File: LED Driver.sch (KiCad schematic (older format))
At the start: 0 parts

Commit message: M3 U7
LED Driver
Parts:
- added C? (x2): C, ~, symbol C
- added D?: DIODESCH, ~, symbol DIODESCH
- added L?: INDUCTOR, ~, symbol INDUCTOR
- added R?: R, ~, symbol R
- added U?: AP5726, symbol AP5726
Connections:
- net String +: now also C?.1, D?.2 (K), U?.5 (OVP)
- net String -: now also R?.1, U?.3 (FB)
- new net: D?.1 (A), L?.2, U?.1 (SW)
- new net +5V: C?.1, L?.1, U?.6 (VIN)
- new net GND: C?.2, C?.2, R?.2, U?.2 (GMND)
- new net LED_EN_PWM: U?.4 (EN)
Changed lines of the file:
@@
 Comment4 ""
 $EndDescr
-Text HLabel 1900 2500 0    60   Input ~ 0
-EN
-Text HLabel 1900 2850 0    60   Input ~ 0
-FREQ
-Text HLabel 3600 2550 0    60   Output ~ 0
+Text HLabel 1800 2000 0    60   Input ~ 0
+LED_EN_PWM
+Text HLabel 10300 900  2    60   Output ~ 0
 String +
-Text HLabel 3600 2800 0    60   Input ~ 0
+Text HLabel 10300 2350 2    60   Input ~ 0
 String -
+$Comp
+L AP5726 U?
+U 1 1 52FE2415
+P 2850 2000
+F 0 "U?" H 3050 1550 60  0000 C CNN
+F 1 "AP5726" H 2850 2050 60  0000 C CNN
+F 2 "" H 2850 2000 60  0000 C CNN
+F 3 "" H 2850 2000 60  0000 C CNN
+	1    2850 2000
+	1    0    0    -1
+$EndComp
+$Comp
+L +5V #PWR?
+U 1 1 52FE3BF3
+P 1850 850
+F 0 "#PWR?" H 1850 940 20  0001 C CNN
+F 1 "+5V" H 1850 940 30  0000 C CNN
+F 2 "" H 1850 850 60  0000 C CNN
+F 3 "" H 1850 850 60  0000 C CNN
+	1    1850 850
+	1    0    0    -1
+$EndComp
+$Comp
+L GND #PWR?
+U 1 1 52FE3C0C
+P 1850 1450
+F 0 "#PWR?" H 1850 1450 30  0001 C CNN
+F 1 "GND" H 1850 1380 30  0001 C CNN
+F 2 "" H 1850 1450 60  0000 C CNN
+F 3 "" H 1850 1450 60  0000 C CNN
+	1    1850 1450
+	1    0    0    -1
+$EndComp
+$Comp
+L GND #PWR?
+U 1 1 52FE3C19
+P 2850 2900
+F 0 "#PWR?" H 2850 2900 30  0001 C CNN
+F 1 "GND" H 2850 2830 30  0001 C CNN
+F 2 "" H 2850 2900 60  0000 C CNN
+F 3 "" H 2850 2900 60  0000 C CNN
+	1    2850 2900
+	1    0    0    -1
+$EndComp
+Wire Wire Line
+	1800 2000 2100 2000
+Wire Wire Line
+	2850 2600 2850 2900
+$Comp
+L C C?
+U 1 1 52FE3C2B
+P 1850 1150
+F 0 "C?" H 1850 1250 40  0000 L CNN
+F 1 "C" H 1856 1065 40  0000 L CNN
+F 2 "~" H 1888 1000 30  0000 C CNN
+F 3 "~" H 1850 1150 60  0000 C CNN
+	1    1850 1150
+	1    0    0    -1
+$EndComp
+Wire Wire Line
+	1850 850  1850 950
+Wire Wire Line
+	1850 1350 1850 1450
+Wire Wire Line
+	1850 900  2750 900
+Wire Wire Line
+	2700 900  2700 1350
+Connection ~ 1850 900
+$Comp
+L INDUCTOR L?
+U 1 1 52FE4086
+P 3050 900
+F 0 "L?" V 3000 900 40  0000 C CNN
+F 1 "INDUCTOR" V 3150 900 40  0000 C CNN
+F 2 "~" H 3050 900 60  0000 C CNN
+F 3 "~" H 3050 900 60  0000 C CNN
+	1    3050 900
+	0    -1   -1   0
+$EndComp
+Connection ~ 2700 900
+Wire Wire Line
+	3350 900  3650 900
+Wire Wire Line
+	3550 900  3550 1150
+Wire Wire Line
+	3550 1150 3200 1150
+Wire Wire Line
+	3200 1150 3200 1350
+$Comp
+L DIODESCH D?
+U 1 1 52FE40A9
+P 3850 900
+F 0 "D?" H 3850 1000 40  0000 C CNN
+F 1 "DIODESCH" H 3850 800 40  0000 C CNN
+F 2 "~" H 3850 900 60  0000 C CNN
+F 3 "~" H 3850 900 60  0000 C CNN
+	1    3850 900
+	1    0    0    -1
+$EndComp
+Connection ~ 3550 900
+$Comp
+L C C?
+U 1 1 52FE40C3
+P 9600 1350
+F 0 "C?" H 9600 1450 40  0000 L CNN
+F 1 "C" H 9606 1265 40  0000 L CNN
+F 2 "~" H 9638 1200 30  0000 C CNN
+F 3 "~" H 9600 1350 60  0000 C CNN
+	1    9600 1350
+	1    0    0    -1
+$EndComp
+Wire Wire Line
+	4050 900  10300 900
+Wire Wire Line
+	9600 900  9600 1150
+$Comp
+L GND #PWR?
+U 1 1 52FE4304
+P 9600 2000
+F 0 "#PWR?" H 9600 2000 30  0001 C CNN
+F 1 "GND" H 9600 1930 30  0001 C CNN
+F 2 "" H 9600 2000 60  0000 C CNN
+F 3 "" H 9600 2000 60  0000 C CNN
+	1    9600 2000
+	1    0    0    -1
+$EndComp
+Wire Wire Line
+	9600 1550 9600 2000
+Connection ~ 9600 900
+$Comp
+L R R?
+U 1 1 52FE4342
+P 4450 2650
+F 0 "R?" V 4530 2650 40  0000 C CNN
+F 1 "R" V 4457 2651 40  0000 C CNN
+F 2 "~" V 4380 2650 30  0000 C CNN
+F 3 "~" H 4450 2650 30  0000 C CNN
+	1    4450 2650
+	1    0    0    -1
+$EndComp
+Wire Wire Line
+	3650 2350 10300 2350
+Wire Wire Line
+	4450 2350 4450 2400
+Wire Wire Line
+	2850 2750 4050 2750
+Wire Wire Line
+	4050 2750 4050 3100
+Wire Wire Line
+	4050 3100 4450 3100
+Wire Wire Line
+	4450 3100 4450 2900
+Connection ~ 2850 2750
+Wire Wire Line
+	3650 2000 4400 2000
+Wire Wire Line
+	4400 2000 4400 900
+Connection ~ 4400 900
+Connection ~ 4450 2350
 $EndSCHEMATC

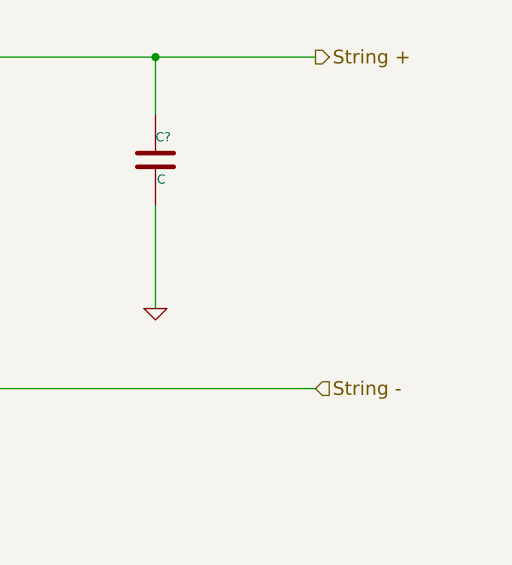
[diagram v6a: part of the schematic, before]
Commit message: M3 U8
Arduino Module.   My Arduino Pin numbering does not matches Chris'.  I
believe he missed one in the video
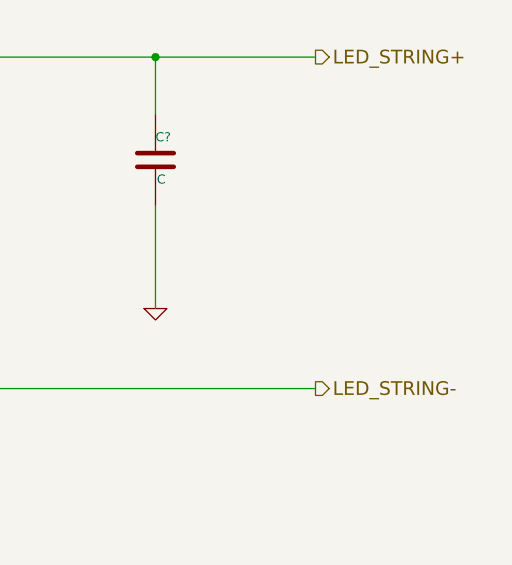
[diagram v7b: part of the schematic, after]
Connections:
- net String + renamed LED_STRING+
- net String - renamed LED_STRING-
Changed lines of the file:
@@
 Sheet 6 9
 Title ""
-Date "14 feb 2014"
+Date "15 feb 2014"
 Rev ""
 Comp ""
@@
 LED_EN_PWM
 Text HLabel 10300 900  2    60   Output ~ 0
-String +
-Text HLabel 10300 2350 2    60   Input ~ 0
-String -
+LED_STRING+
+Text HLabel 10300 2350 2    60   Output ~ 0
+LED_STRING-
 $Comp
 L AP5726 U?
